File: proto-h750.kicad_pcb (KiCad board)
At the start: 2 copper layers, 63.5 x 59.7 mm, 43 parts, among them J1 Micro_SD_Card, J2 USB_B_Micro, J3 USB_B_Micro, J4 Conn_02x14_Odd_Even, J5 Conn_02x14_Odd_Even, J6 Conn_02x08_Odd_Even, J7 Conn_02x02_Odd_Even, J8 USB_B_Micro, SW1 SW_Push, SW2 SW_Push, SW3 SW_DIP_x01, U1 S25FL132K0XMFI010, U2 STM32H750VBT6, U3 AP1117-33, Y1 8MHz, Y2 32.768KHz

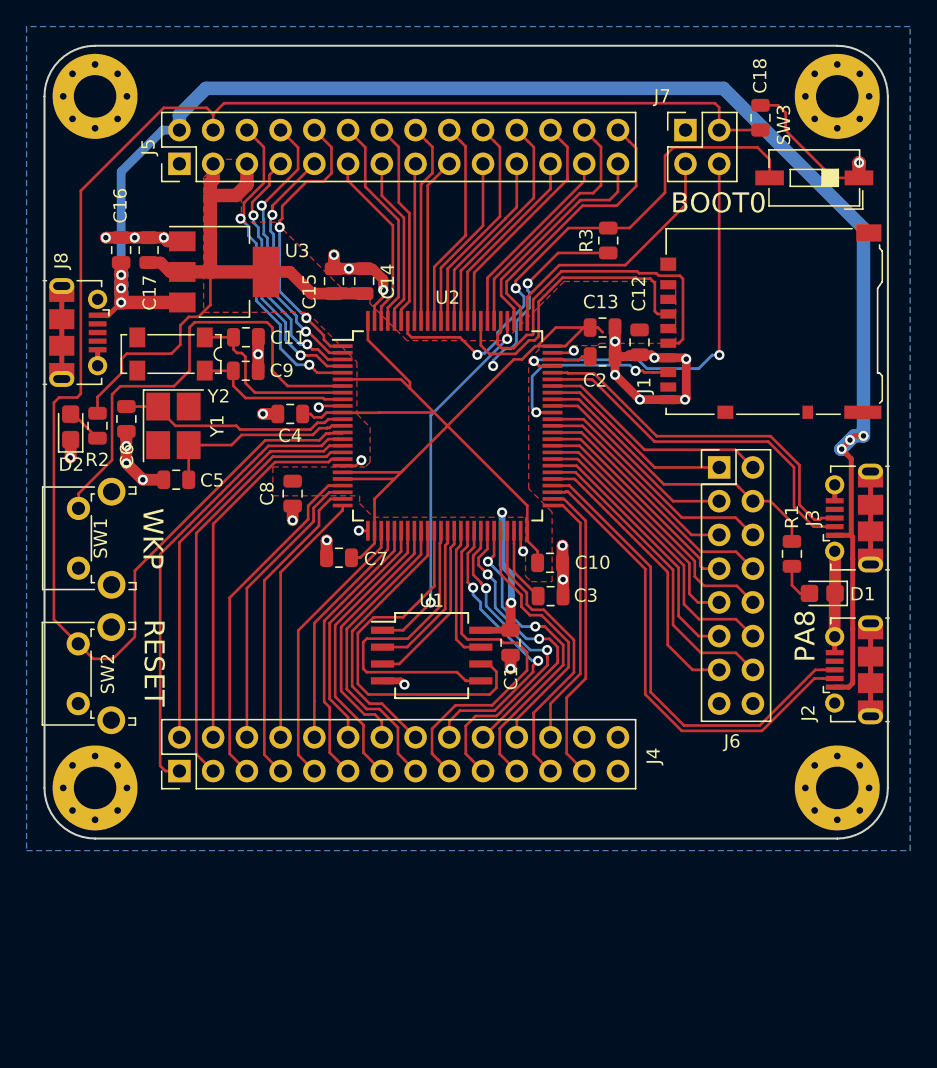
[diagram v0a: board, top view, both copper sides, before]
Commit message: Add eth phy
Signed-off-by: Martin Ribelotta <martinribelotta@gmail.com>
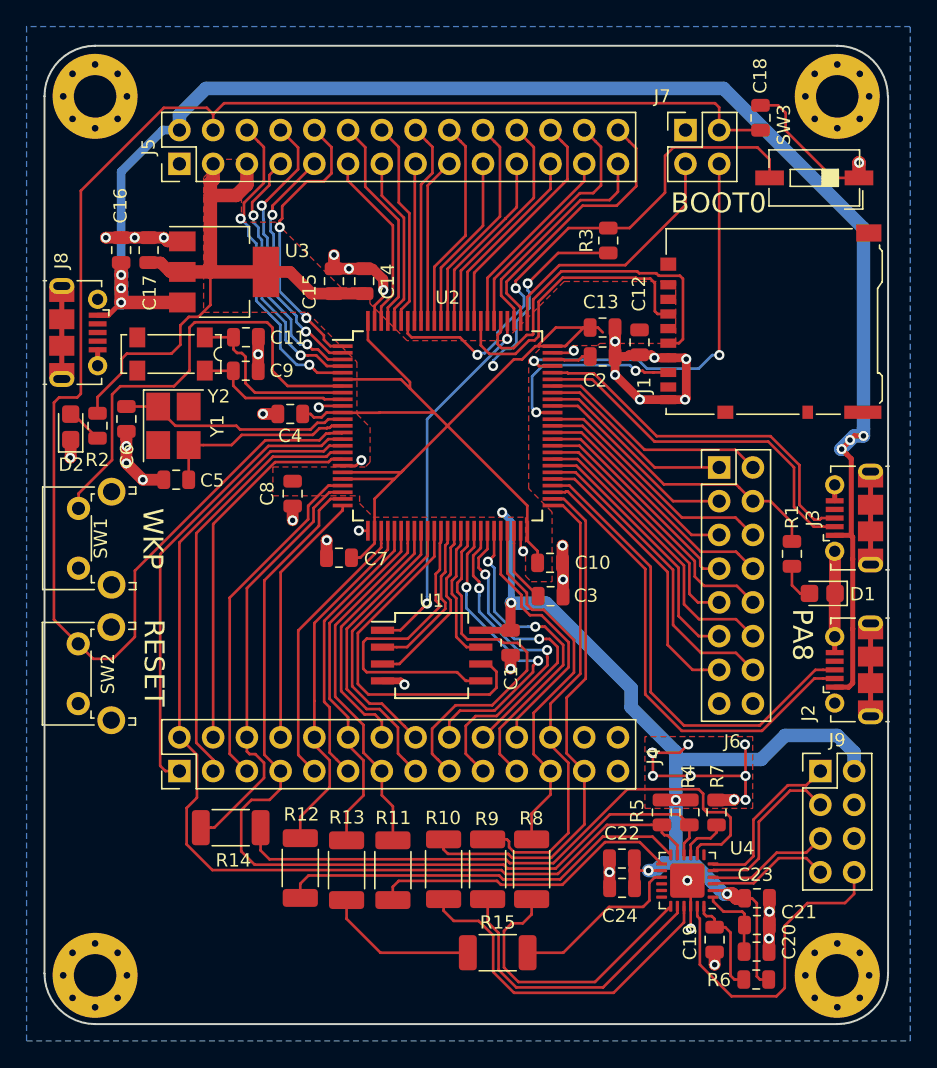
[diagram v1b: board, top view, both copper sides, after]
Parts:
- added C19: 0.1u, Capacitor_SMD:C_0805_2012Metric, F.Cu at (149.5, 109.2)
- added C20: 2.2u, Capacitor_SMD:C_0805_2012Metric, F.Cu at (152.7, 110.1)
- added C21: 4.7u, Capacitor_SMD:C_0805_2012Metric, F.Cu at (152.7, 108.1)
- added C22: 0.1u, Capacitor_SMD:C_0805_2012Metric, F.Cu at (142.5, 103.1)
- added C23: 0.1u, Capacitor_SMD:C_0805_2012Metric, F.Cu at (152.7, 106.1)
- added C24: 4.7u, Capacitor_SMD:C_0805_2012Metric, F.Cu at (142.5, 105.3)
- added J9: Conn_02x04_Odd_Even, Connector_PinHeader_2.54mm:PinHeader_2x04_P2.54mm_Vertical, F.Cu at (157.5, 96.5)
- added R10: 22R, Resistor_SMD:R_2010_5025Metric, F.Cu at (129.1, 103.9)
- added R11: 22R, Resistor_SMD:R_2010_5025Metric, F.Cu at (125.3, 104.0)
- added R12: 22R, Resistor_SMD:R_2010_5025Metric, F.Cu at (118.3, 103.8)
- added R13: 22R, Resistor_SMD:R_2010_5025Metric, F.Cu at (121.8, 104.0)
- added R14: 22R, Resistor_SMD:R_2010_5025Metric, F.Cu at (113.1, 100.8)
- added R15: 22R, Resistor_SMD:R_2010_5025Metric, F.Cu at (133.2, 110.2)
- added R4: 10K, Resistor_SMD:R_0805_2012Metric, F.Cu at (147.6, 99.6)
- added R5: 10K, Resistor_SMD:R_0805_2012Metric, F.Cu at (145.5, 99.6)
- added R6: 10K, Resistor_SMD:R_0805_2012Metric, F.Cu at (152.6, 112.2)
- added R7: 6.49K 1%, Resistor_SMD:R_0805_2012Metric, F.Cu at (149.7, 99.6)
- added R8: 22R, Resistor_SMD:R_2010_5025Metric, F.Cu at (135.7, 103.9)
- added R9: 22R, Resistor_SMD:R_2010_5025Metric, F.Cu at (132.4, 103.9)
- added U4: KSZ8081RNA, Package_DFN_QFN:QFN-24-1EP_4x4mm_P0.5mm_EP2.6x2.6mm, F.Cu at (147.5, 104.8)
- moved H3 14.1 mm to (102.9, 111.9)
- moved H4 14.1 mm to (158.8, 111.9)
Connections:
- net /PA2 renamed /ENET_MDIO
- net /PC1 renamed /ENET_MDC
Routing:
- net VCC: track 153.1 -> 219.0 mm, vias 4 -> 7
- net /ENET_MDC: track 30.0 -> 80.0 mm
- net /ENET_MDIO: track 24.0 -> 70.8 mm
- net /ENET_CLK: track 0.00 -> 46.1 mm
- net /ENET_RXD1: track 0.00 -> 31.2 mm
- net GND: track 102.0 -> 133.0 mm, vias 30 -> 45
- net /ENET_TXD1: track 0.00 -> 26.6 mm
- net /ETH_LED: track 0.00 -> 24.6 mm
- net /ENET_RXD0: track 0.00 -> 23.6 mm
- net /ENET_TXD0: track 0.00 -> 22.5 mm
- net /ENET_TXEN: track 0.00 -> 21.9 mm
- net /PB13: track 23.2 -> 39.9 mm
- net /PB12: track 19.7 -> 34.8 mm
- net /ENET_CRSDV: track 0.00 -> 13.2 mm
- net /ETH_TX+: track 0.00 -> 12.6 mm
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- added copper zone on F.Cu, net GND
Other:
- board size 63.5 x 59.7 mm -> 63.5 x 73.7 mm

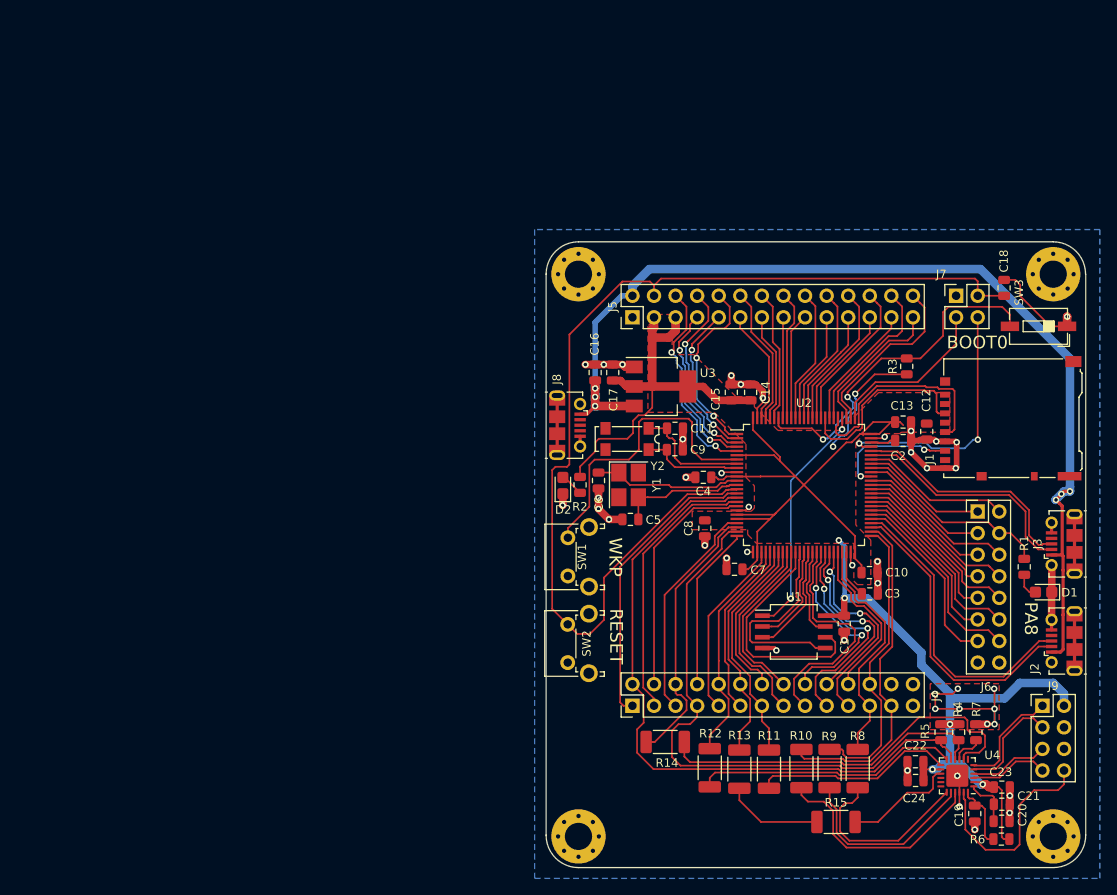
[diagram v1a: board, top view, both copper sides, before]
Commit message: Add README, create schematics and put measures in PCB
Signed-off-by: Martin Ribelotta <martinribelotta@gmail.com>
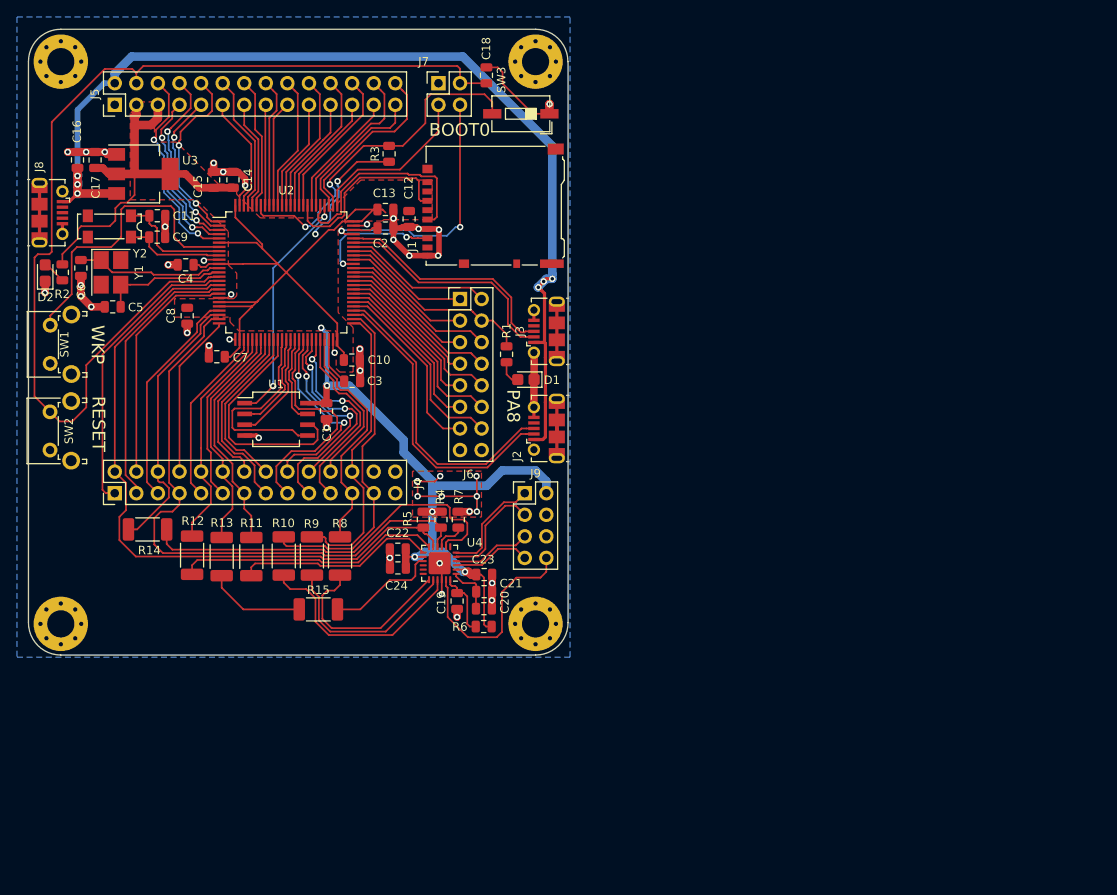
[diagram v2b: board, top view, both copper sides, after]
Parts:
- moved C2 65.9 mm to (80.1, 40.3)
- moved C21 65.9 mm to (91.8, 83.1)
- moved J6 65.9 mm to (88.9, 48.6)
- moved R1 65.9 mm to (94.4, 55.1)
- moved C1 65.9 mm to (73.2, 61.8)
- moved C11 65.9 mm to (53.3, 38.8)
- moved C16 65.9 mm to (43.9, 32.3)
- moved C17 65.9 mm to (46.0, 32.3)
- moved C18 65.9 mm to (92.0, 22.3)
- moved C23 65.9 mm to (91.8, 81.1)
- moved C24 65.9 mm to (81.6, 80.3)
- moved C4 65.9 mm to (56.6, 44.6)
- moved C5 65.9 mm to (48.0, 49.6)
- moved C7 65.9 mm to (60.3, 55.4)
- moved C8 65.9 mm to (56.8, 50.6)
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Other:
- outline, holes or cut-outs redrawn

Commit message: Change dimention annotations
Signed-off-by: Martin Ribelotta <martinribelotta@gmail.com>
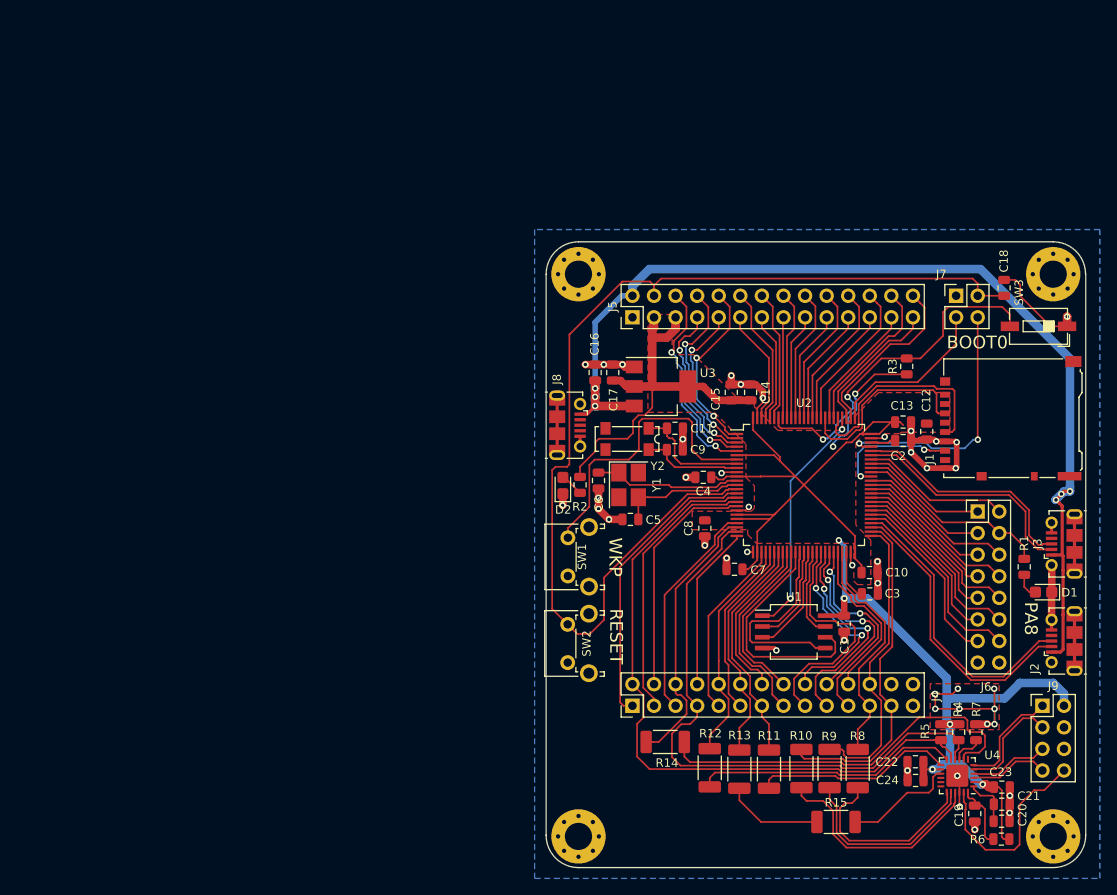
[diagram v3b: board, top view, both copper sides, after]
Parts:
- moved C2 65.9 mm to (141.1, 65.3)
- moved C21 65.9 mm to (152.7, 108.1)
- moved J6 65.9 mm to (149.9, 73.7)
- moved R1 65.9 mm to (155.3, 80.2)
- moved C1 65.9 mm to (134.2, 86.9)
- moved C11 65.9 mm to (114.2, 63.9)
- moved C16 65.9 mm to (104.8, 57.3)
- moved C17 65.9 mm to (106.9, 57.3)
- moved C18 65.9 mm to (153.0, 47.3)
- moved C23 65.9 mm to (152.7, 106.1)
- moved C24 65.9 mm to (142.5, 105.3)
- moved C4 65.9 mm to (117.6, 69.6)
- moved C5 65.9 mm to (109.0, 74.6)
- moved C7 65.9 mm to (121.2, 80.5)
- moved C8 65.9 mm to (117.7, 75.6)
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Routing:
- net /USB0_D-: track 35.9 -> 34.7 mm
- net /USB0_D+: track 36.0 -> 34.8 mm
- net /ETH_LED: track 24.6 -> 23.7 mm
- net /ENET_TXEN: track 21.9 -> 22.7 mm
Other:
- outline, holes or cut-outs redrawn

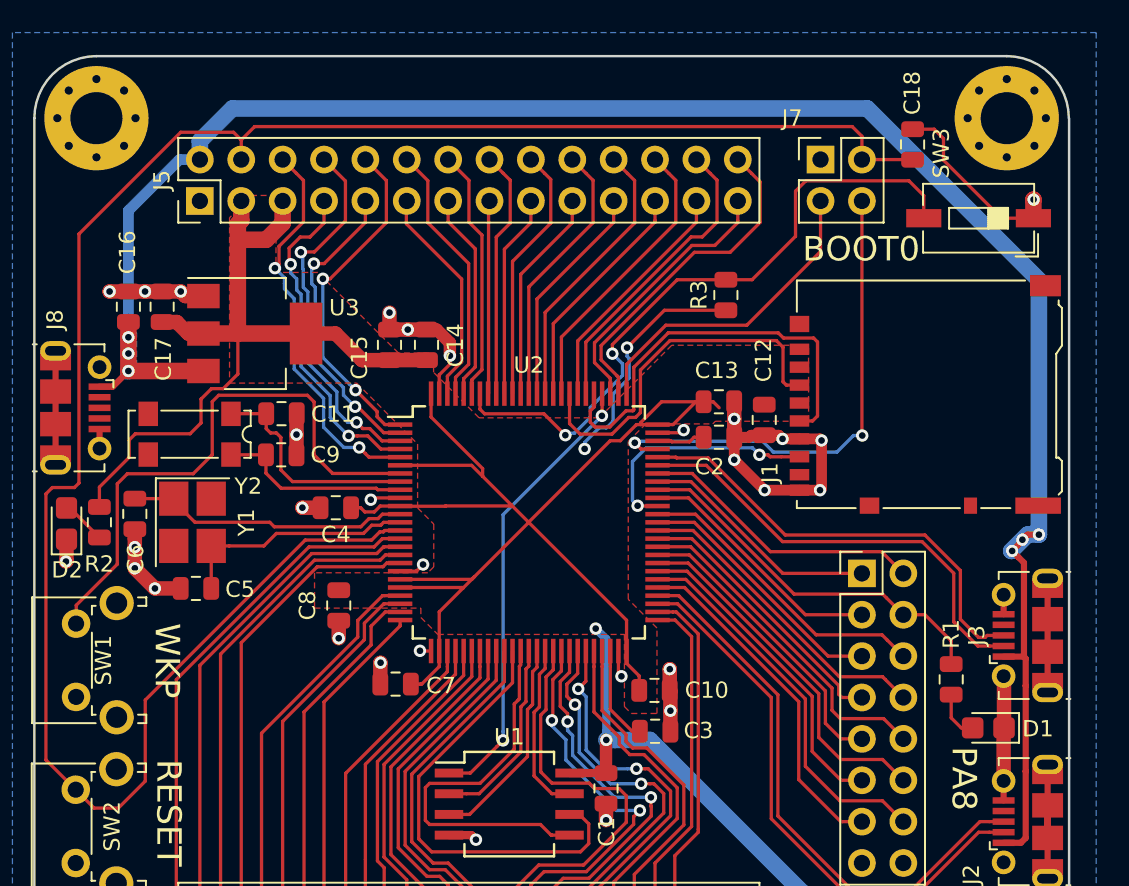
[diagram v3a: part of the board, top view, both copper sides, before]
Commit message: Prepare to BOM
 - Change BOOT switch by jumper
 - Change 32.768KHz footprint by 2SMD 2.0x1.2mm
 - Change 8MHz 4SMD by same footprint in 16MHz
 - Add Part number field of all schematic items

Signed-off-by: Martin Ribelotta <martinribelotta@gmail.com>
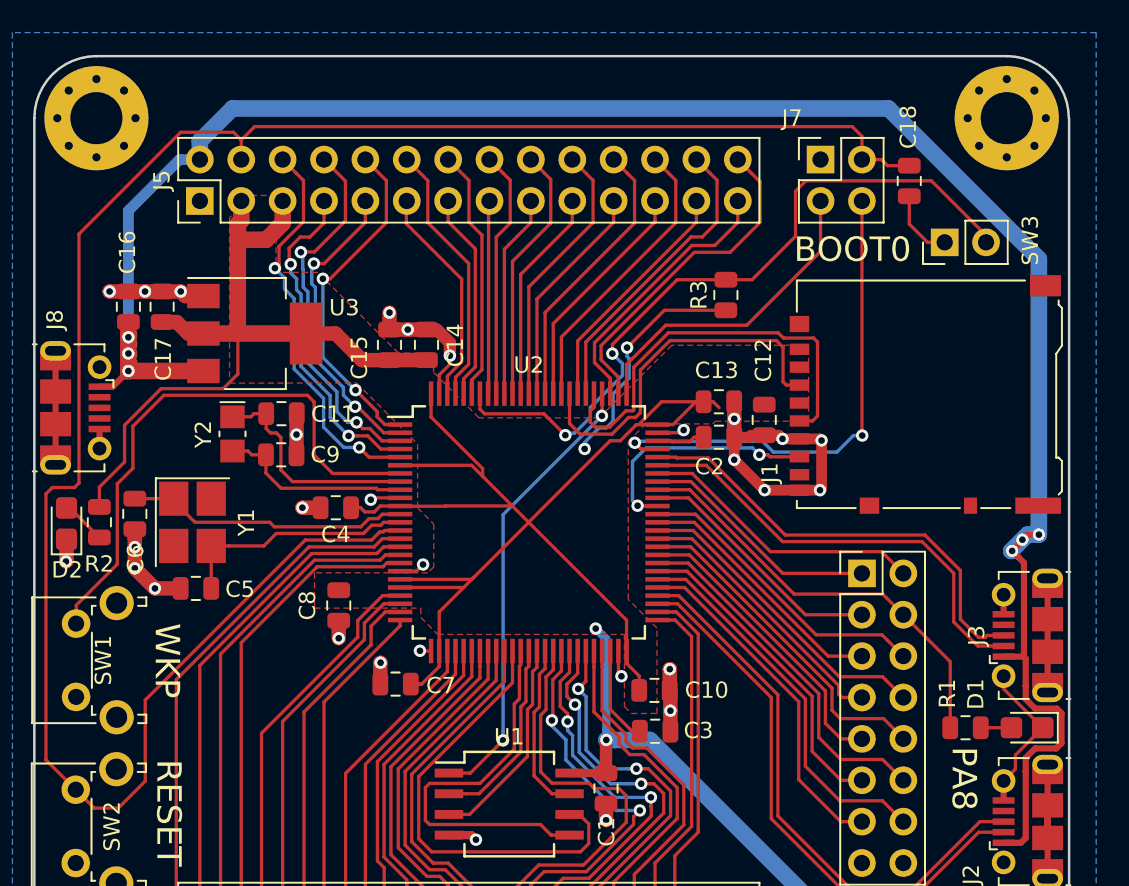
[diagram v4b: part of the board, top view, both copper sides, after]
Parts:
- SW3: footprint Button_Switch_SMD:SW_DIP_SPSTx01_Slide_6.7x4.1mm_W6.73mm_P2.54mm_LowProfile_JPin -> Connector_PinHeader_2.54mm:PinHeader_1x02_P2.54mm_Vertical
- Y1: value 8MHz -> 16MHz
- Y2: footprint Crystal:Crystal_SMD_SeikoEpson_MC156-4Pin_7.1x2.5mm -> Crystal:Crystal_SMD_MicroCrystal_CC8V-T1A-2Pin_2.0x1.2mm_HandSoldering
- moved R1 3.10 mm to (156.2, 83.1), turned to 180 degrees
- moved Y2 2.63 mm to (111.2, 65.1), turned to 270 degrees
- moved SW3 2.55 mm to (154.9, 53.3), turned to 90 degrees
- moved D1 2.38 mm to (160.0, 83.1)
- moved C18 2.25 mm to (152.8, 49.6), turned to 270 degrees
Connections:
- Y2 pad 2: Net-(Y2-Pad2) -> Net-(C9-Pad2)
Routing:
- net GND: track 133.0 -> 127.8 mm, vias 45 -> 44
- net +5V: track 123.7 -> 127.9 mm
- net /BOOT: track 41.0 -> 44.9 mm
- net /PA8: track 23.3 -> 26.4 mm
- net Net-(D1-Pad2): track 3.00 -> 1.88 mm
